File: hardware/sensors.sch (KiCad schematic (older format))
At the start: 19 parts, among them U1 LM358, U2 MCP6001, U3 LAH-100P, U4 LOC110, U5 MCP6001, U6 MCP6001

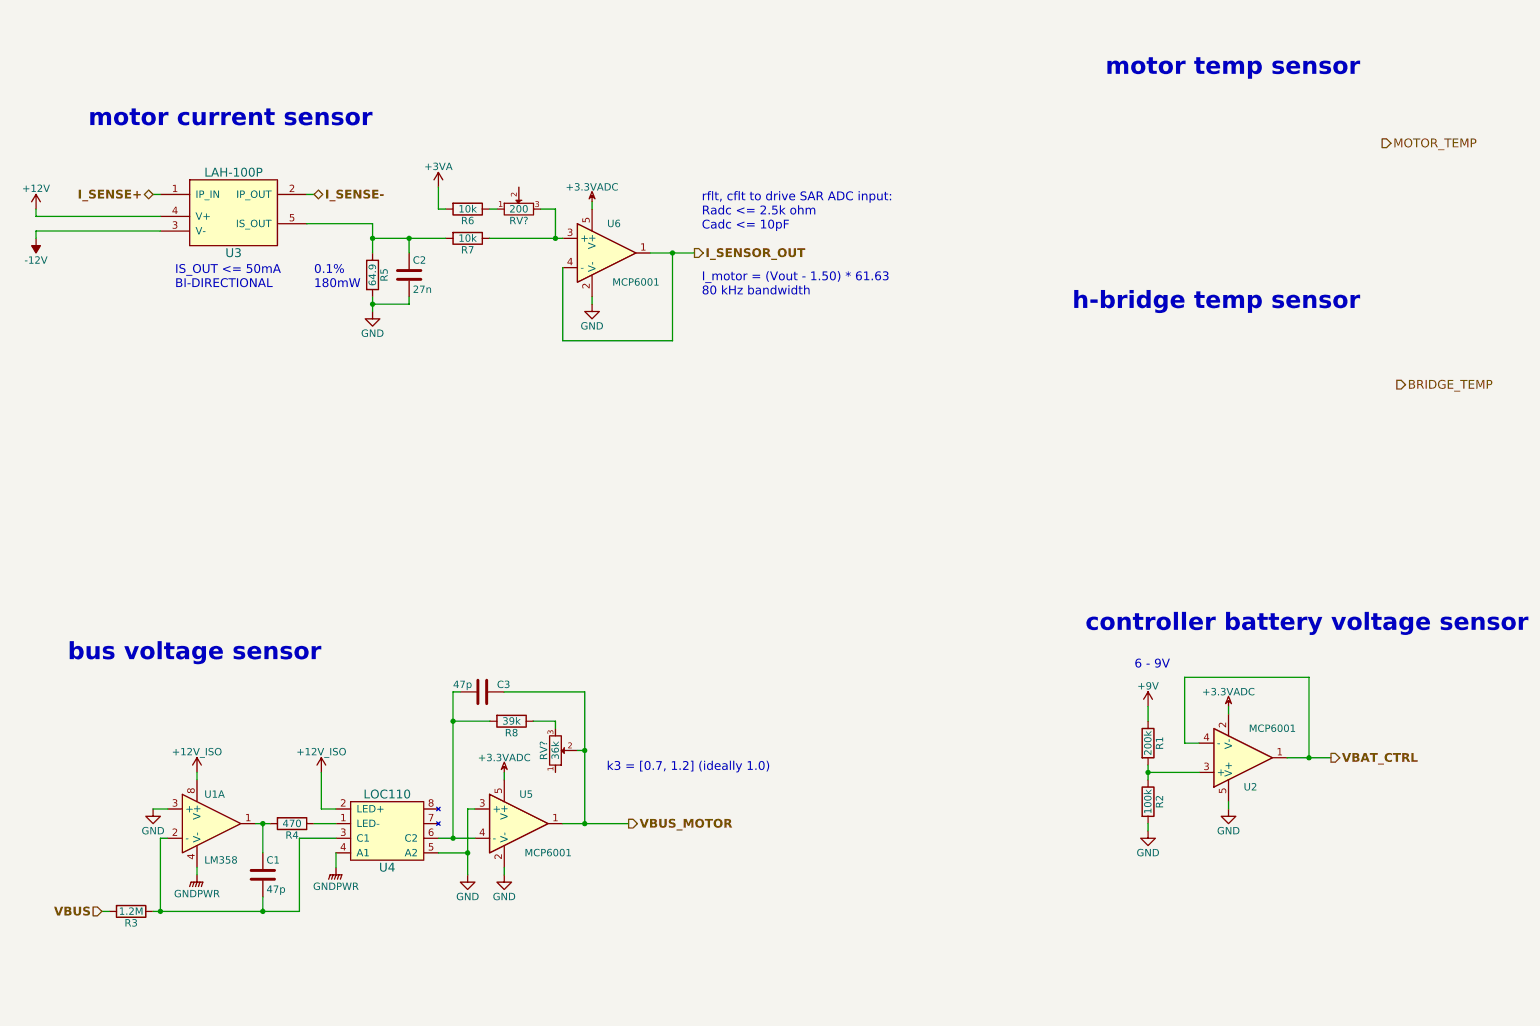
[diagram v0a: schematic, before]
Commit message: Update sensors, hbridge caps, add heatsink
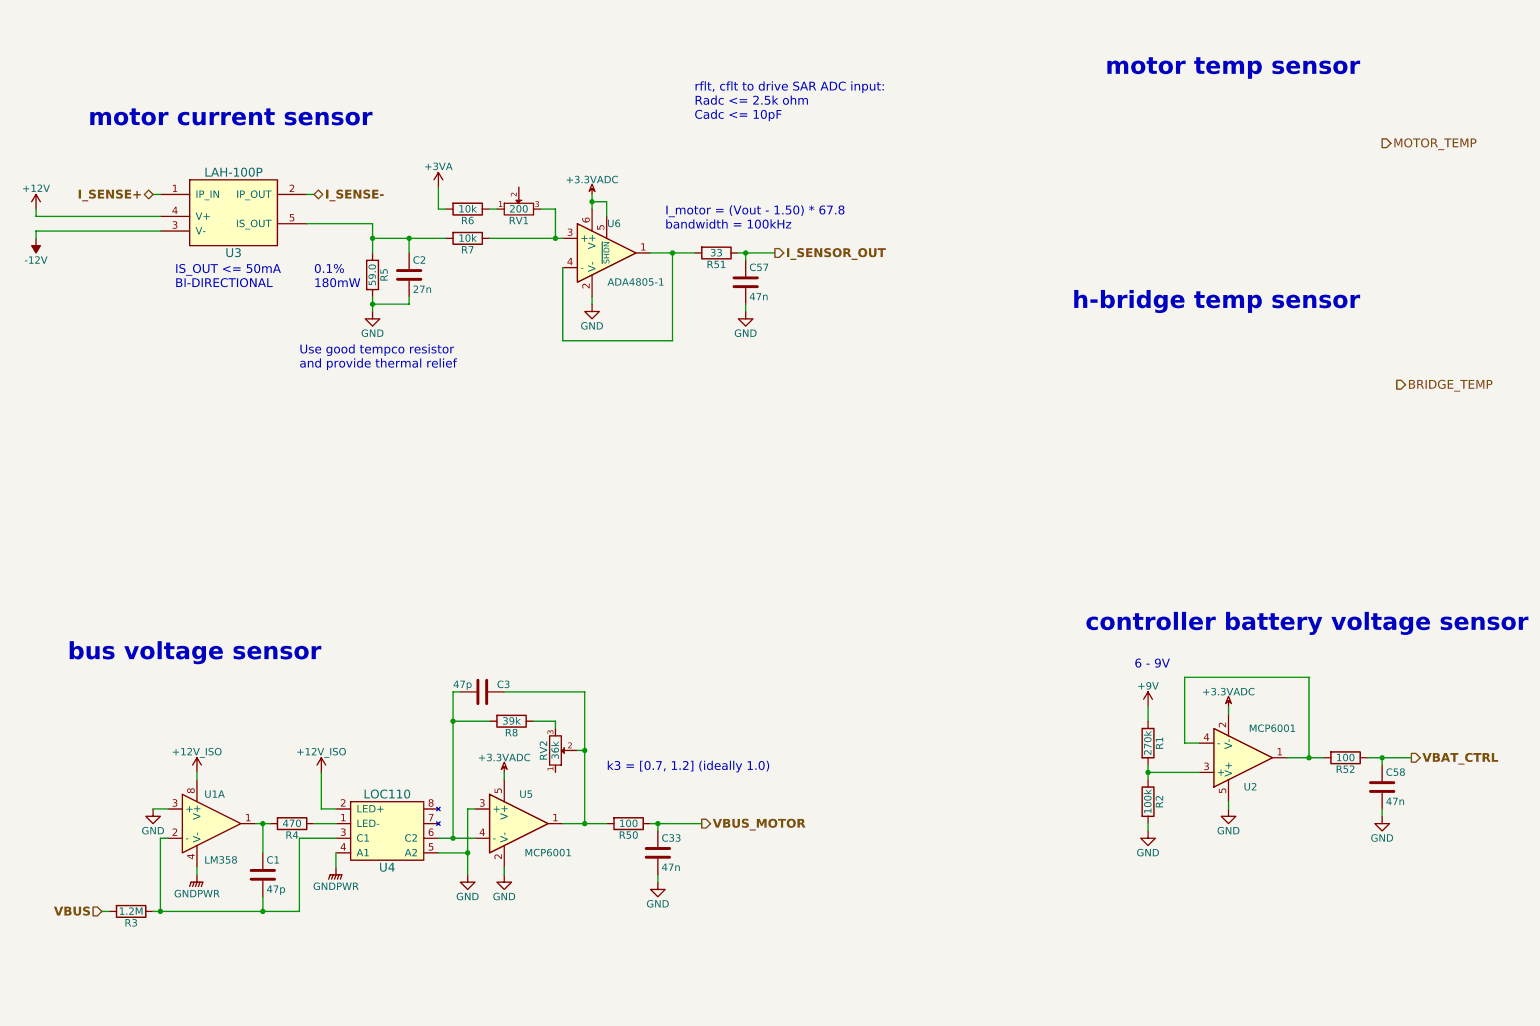
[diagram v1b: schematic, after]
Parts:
- removed U6: MCP6001, TO_SOT_Packages_SMD:SC-70-5, symbol MCP6001
- added C33, C57, C58: 47n, symbol C
- added R50, R52: 100, symbol R
- added R51: 33, symbol R
- added U6: ADA4805-1, symbol ADA4805-1
- R1: value 200k -> 270k
- R5: value 64.9 -> 59.0
- gave numbers to parts that had none: 2
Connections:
- net +3.3VADC: now also U6.5 (~SHDN), U6.6 (V+)
- net GND: now also C33.2, C57.2, C58.2, U6.2 (V-)
- net I_SENSOR_OUT: now also C57.1, R51.1
- net VBAT_CTRL: now also C58.1, R52.1; no longer U2.1, U2.4 (-)
- net VBUS_MOTOR: now also C33.1, R50.1; no longer C3.1, RV2.2, U5.1
- net at R7.1, RV1.3: now also U6.3 (+)
- new net: R52.2, U2.1, U2.4 (-)
- new net: C3.1, R50.2, RV2.2, U5.1
- new net: R51.2, U6.1, U6.4 (-)
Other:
- note added: "I_motor = (Vout - 1.50) * 67.8\nbandwidth = 100kHz"
- note added: "Use good tempco resistor\nand provide thermal relief"
- note removed: "I_motor = (Vout - 1.50) * 61.63\n80 kHz bandwidth"

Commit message: Layout first draft
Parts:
- C33, C57, C58: footprint (none) -> Capacitors_SMD:C_0603
- U6: footprint (none) -> TO_SOT_Packages_SMD:SOT-23-6
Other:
- note added: "0.05%\n180mW"
- note removed: "0.1%\n180mW"
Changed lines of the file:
@@
 I_motor = (Vout - 1.50) * 67.8\nbandwidth = 100kHz
 Text Notes 2750 2550 0    60   ~ 0
-0.1%\n180mW
+0.05%\n180mW
 $Comp
 L +3VA #PWR013
@@
 F 0 "C57" H 5725 2600 50  0000 L CNN
 F 1 "47n" H 5725 2400 50  0000 L CNN
-F 2 "" H 5738 2350 50  0001 C CNN
+F 2 "Capacitors_SMD:C_0603" H 5738 2350 50  0001 C CNN
 F 3 "" H 5700 2500 50  0000 C CNN
 	1    5700 2500
@@
 F 0 "U6" H 4800 2500 50  0000 C CNN
 F 1 "ADA4805-1" H 4950 2100 50  0000 C CNN
-F 2 "" H 4700 2400 50  0001 C CNN
+F 2 "TO_SOT_Packages_SMD:SOT-23-6" H 4700 2400 50  0001 C CNN
 F 3 "" H 4800 2500 50  0000 C CNN
 	1    4750 2300
@@
 F 0 "C33" H 5125 6500 50  0000 L CNN
 F 1 "47n" H 5125 6300 50  0000 L CNN
-F 2 "" H 5138 6250 50  0001 C CNN
+F 2 "Capacitors_SMD:C_0603" H 5138 6250 50  0001 C CNN
 F 3 "" H 5100 6400 50  0000 C CNN
 	1    5100 6400
@@
 F 0 "C58" H 10075 6050 50  0000 L CNN
 F 1 "47n" H 10075 5850 50  0000 L CNN
-F 2 "" H 10088 5800 50  0001 C CNN
+F 2 "Capacitors_SMD:C_0603" H 10088 5800 50  0001 C CNN
 F 3 "" H 10050 5950 50  0000 C CNN
 	1    10050 5950

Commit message: revised power layout
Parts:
- U3: footprint (none) -> 2kwMotorController:LAH_100-P
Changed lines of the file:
@@
 F 0 "U3" H 2200 1700 60  0000 C CNN
 F 1 "LAH-100P" H 2200 2250 60  0000 C CNN
-F 2 "" H 2200 2000 60  0001 C CNN
+F 2 "2kwMotorController:LAH_100-P" H 2200 2000 60  0001 C CNN
 F 3 "" H 2200 2000 60  0000 C CNN
 	1    2200 2000

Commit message: Added most footprints, did non-power layout
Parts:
- R50, R51, R52: footprint (none) -> Resistors_SMD:R_0603
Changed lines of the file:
@@
 F 0 "R51" V 5580 2300 50  0000 C CNN
 F 1 "33" V 5500 2300 50  0000 C CNN
-F 2 "" V 5430 2300 50  0001 C CNN
+F 2 "Resistors_SMD:R_0603" V 5430 2300 50  0001 C CNN
 F 3 "" H 5500 2300 50  0000 C CNN
 	1    5500 2300
@@
 F 0 "R50" V 4980 6200 50  0000 C CNN
 F 1 "100" V 4900 6200 50  0000 C CNN
-F 2 "" V 4830 6200 50  0001 C CNN
+F 2 "Resistors_SMD:R_0603" V 4830 6200 50  0001 C CNN
 F 3 "" H 4900 6200 50  0000 C CNN
 	1    4900 6200
@@
 F 0 "R52" V 9880 5750 50  0000 C CNN
 F 1 "100" V 9800 5750 50  0000 C CNN
-F 2 "" V 9730 5750 50  0001 C CNN
+F 2 "Resistors_SMD:R_0603" V 9730 5750 50  0001 C CNN
 F 3 "" H 9800 5750 50  0000 C CNN
 	1    9800 5750

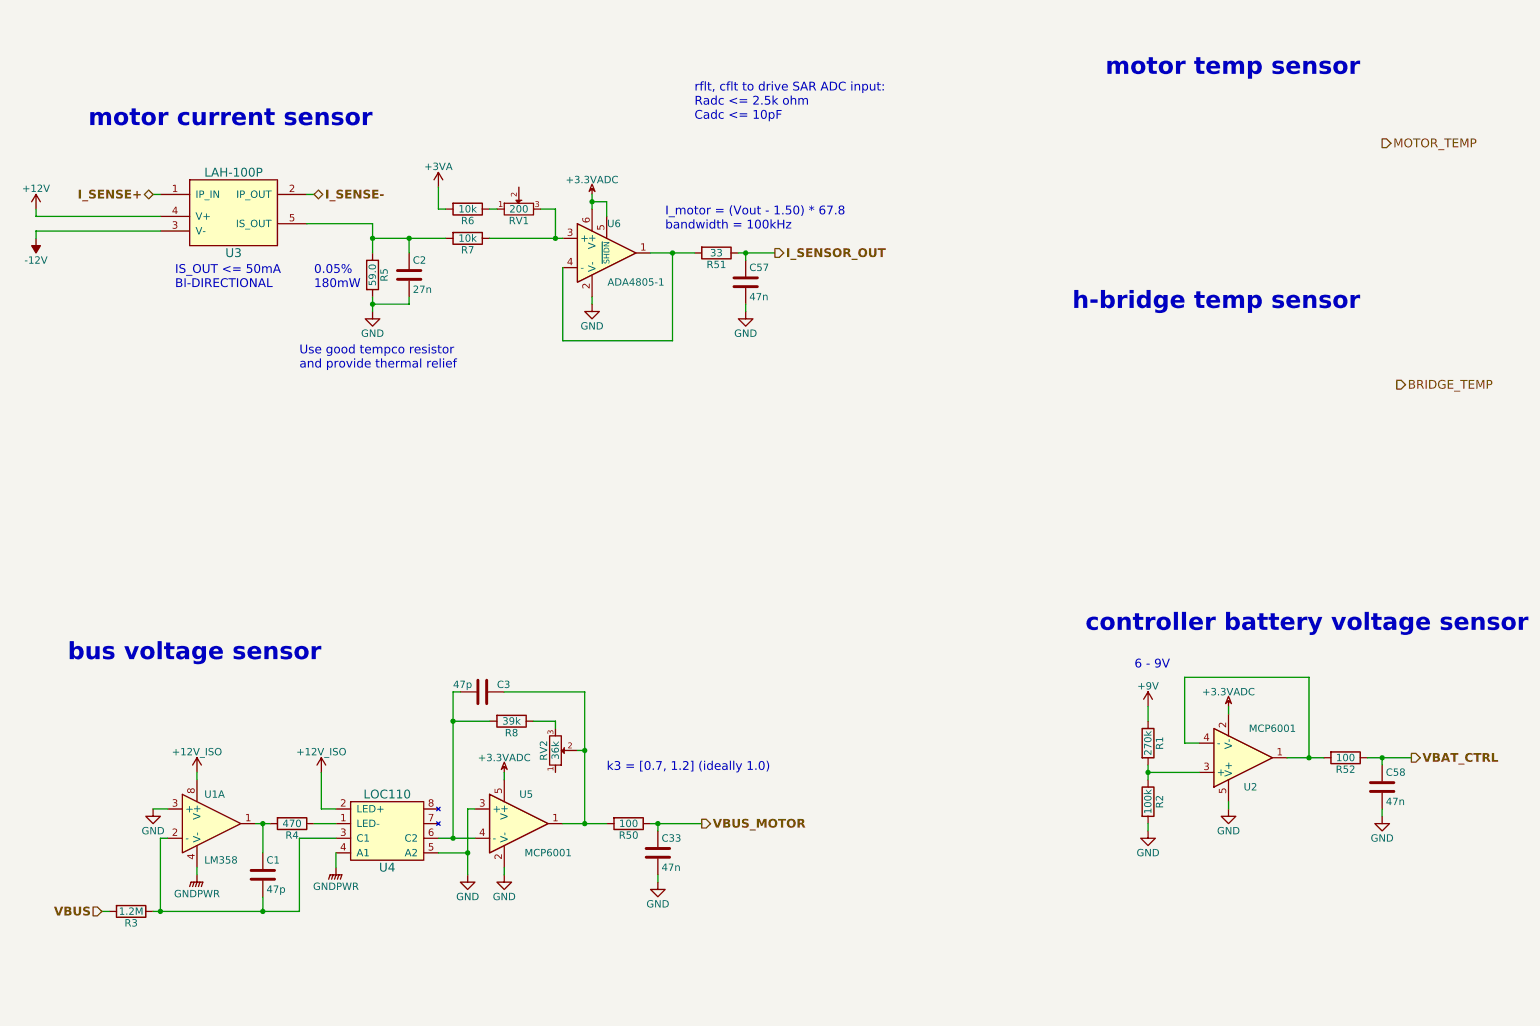
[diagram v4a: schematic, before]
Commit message: H-bridge decoupling, footprints, mechanical
- Finished H-bridge decoupling study and chose H-bridge caps
- Changed LT3471 inductors to those found in reference design,
  made footprints for them
- Swapped Si86xx isolator for Si80xx (smaller package)
- Updated heatsink footprint with correct screw sizes
- Created mechanical hole footprints (M3, M4 screws)
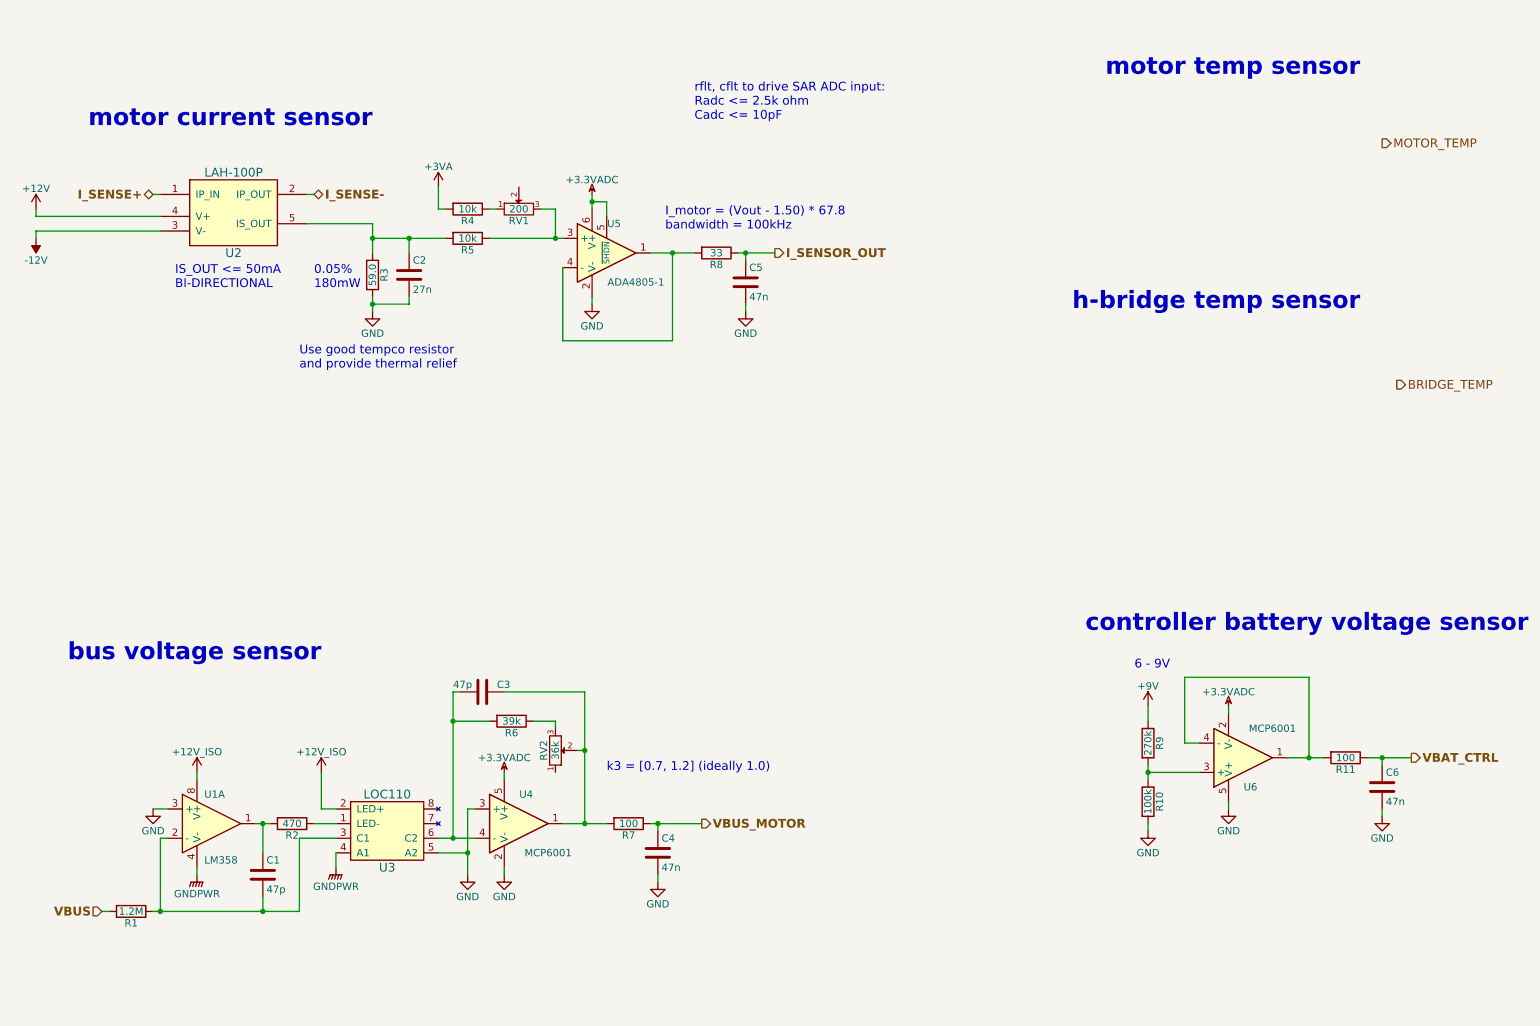
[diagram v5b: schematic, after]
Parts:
- renumbered C33 to C4, C57 to C5, C58 to C6, R3 to R1, R2 to R10, R52 to R11, R4 to R2, R5 to R3, R6 to R4, R7 to R5, R8 to R6, R50 to R7, R51 to R8, R1 to R9, U3 to U2, U4 to U3, U5 to U4, U6 to U5, U2 to U6
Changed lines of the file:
@@
 $EndDescr
 $Comp
-L LAH-100P U3
+L LAH-100P U2
 U 1 1 5975C20B
 P 2200 2000
-F 0 "U3" H 2200 1700 60  0000 C CNN
+F 0 "U2" H 2200 1700 60  0000 C CNN
 F 1 "LAH-100P" H 2200 2250 60  0000 C CNN
 F 2 "2kwMotorController:LAH_100-P" H 2200 2000 60  0001 C CNN
@@
 $EndComp
 $Comp
-L R R5
+L R R3
 U 1 1 5975C452
 P 3150 2450
-F 0 "R5" V 3230 2450 50  0000 C CNN
+F 0 "R3" V 3230 2450 50  0000 C CNN
 F 1 "59.0" V 3150 2450 50  0000 C CNN
 F 2 "Resistors_SMD:R_0603" V 3080 2450 50  0001 C CNN
@@
 $EndComp
 $Comp
-L R R7
+L R R5
 U 1 1 5975C99C
 P 3800 2200
-F 0 "R7" V 3880 2200 50  0000 C CNN
+F 0 "R5" V 3880 2200 50  0000 C CNN
 F 1 "10k" V 3800 2200 50  0000 C CNN
 F 2 "Resistors_SMD:R_0603" V 3730 2200 50  0001 C CNN
@@
 $EndComp
 $Comp
-L R R6
+L R R4
 U 1 1 5975CA28
 P 3800 2000
-F 0 "R6" V 3880 2000 50  0000 C CNN
+F 0 "R4" V 3880 2000 50  0000 C CNN
 F 1 "10k" V 3800 2000 50  0000 C CNN
 F 2 "Resistors_SMD:R_0603" V 3730 2000 50  0001 C CNN
@@
 6 - 9V
 $Comp
-L R R1
+L R R9
 U 1 1 597CFA75
 P 8450 5650
-F 0 "R1" V 8530 5650 50  0000 C CNN
+F 0 "R9" V 8530 5650 50  0000 C CNN
 F 1 "270k" V 8450 5650 50  0000 C CNN
 F 2 "Resistors_SMD:R_0603" V 8380 5650 50  0001 C CNN
@@
 $EndComp
 $Comp
-L R R2
+L R R10
 U 1 1 597CFAC7
 P 8450 6050
-F 0 "R2" V 8530 6050 50  0000 C CNN
+F 0 "R10" V 8530 6050 50  0000 C CNN
 F 1 "100k" V 8450 6050 50  0000 C CNN
 F 2 "Resistors_SMD:R_0603" V 8380 6050 50  0001 C CNN
@@
 $EndComp
 $Comp
-L MCP6001 U2
+L MCP6001 U6
 U 1 1 597CFF4C
 P 9100 5750
-F 0 "U2" H 9150 5950 50  0000 C CNN
+F 0 "U6" H 9150 5950 50  0000 C CNN
 F 1 "MCP6001" H 9300 5550 50  0000 C CNN
 F 2 "TO_SOT_Packages_SMD:SC-70-5" H 9050 5850 50  0001 C CNN
@@
 VBUS_MOTOR
 $Comp
-L R R4
+L R R2
 U 1 1 597E87B7
 P 2600 6200
-F 0 "R4" V 2680 6200 50  0000 C CNN
+F 0 "R2" V 2680 6200 50  0000 C CNN
 F 1 "470" V 2600 6200 50  0000 C CNN
 F 2 "Resistors_SMD:R_0603" V 2530 6200 50  0001 C CNN
@@
 $EndComp
 $Comp
-L LOC110 U4
+L LOC110 U3
 U 1 1 597E8D03
 P 3250 6250
-F 0 "U4" H 3250 6000 60  0000 C CNN
+F 0 "U3" H 3250 6000 60  0000 C CNN
 F 1 "LOC110" H 3250 6500 60  0000 C CNN
 F 2 "Housings_DIP:DIP-8_W7.62mm" H 3400 6050 60  0001 C CNN
@@
 $EndComp
 $Comp
-L R R3
+L R R1
 U 1 1 597E9880
 P 1500 6800
-F 0 "R3" V 1580 6800 50  0000 C CNN
+F 0 "R1" V 1580 6800 50  0000 C CNN
 F 1 "1.2M" V 1500 6800 50  0000 C CNN
 F 2 "Resistors_SMD:R_0603" V 1430 6800 50  0001 C CNN
@@
 $EndComp
 $Comp
-L MCP6001 U5
+L MCP6001 U4
 U 1 1 597EAA48
 P 4150 6200
-F 0 "U5" H 4200 6400 50  0000 C CNN
+F 0 "U4" H 4200 6400 50  0000 C CNN
 F 1 "MCP6001" H 4350 6000 50  0000 C CNN
 F 2 "TO_SOT_Packages_SMD:SC-70-5" H 4100 6300 50  0001 C CNN
@@
 $EndComp
 $Comp
-L R R8
+L R R6
 U 1 1 597EB265
 P 4100 5500
-F 0 "R8" V 4180 5500 50  0000 C CNN
+F 0 "R6" V 4180 5500 50  0000 C CNN
 F 1 "39k" V 4100 5500 50  0000 C CNN
 F 2 "Resistors_SMD:R_0603" V 4030 5500 50  0001 C CNN
@@
 Use good tempco resistor\nand provide thermal relief
 $Comp
-L R R51
+L R R8
 U 1 1 59B94C38
 P 5500 2300
-F 0 "R51" V 5580 2300 50  0000 C CNN
+F 0 "R8" V 5580 2300 50  0000 C CNN
 F 1 "33" V 5500 2300 50  0000 C CNN
 F 2 "Resistors_SMD:R_0603" V 5430 2300 50  0001 C CNN
@@
 $EndComp
 $Comp
-L C C57
+L C C5
 U 1 1 59B94C8F
 P 5700 2500
-F 0 "C57" H 5725 2600 50  0000 L CNN
+F 0 "C5" H 5725 2600 50  0000 L CNN
 F 1 "47n" H 5725 2400 50  0000 L CNN
 F 2 "Capacitors_SMD:C_0603" H 5738 2350 50  0001 C CNN
@@
 Connection ~ 5700 2300
 $Comp
-L ADA4805-1 U6
+L ADA4805-1 U5
 U 1 1 59B96B07
 P 4750 2300
-F 0 "U6" H 4800 2500 50  0000 C CNN
+F 0 "U5" H 4800 2500 50  0000 C CNN
 F 1 "ADA4805-1" H 4950 2100 50  0000 C CNN
 F 2 "TO_SOT_Packages_SMD:SOT-23-6" H 4700 2400 50  0001 C CNN
@@
 Connection ~ 4650 1950
 $Comp
-L R R50
+L R R7
 U 1 1 59B9903C
 P 4900 6200
-F 0 "R50" V 4980 6200 50  0000 C CNN
+F 0 "R7" V 4980 6200 50  0000 C CNN
 F 1 "100" V 4900 6200 50  0000 C CNN
 F 2 "Resistors_SMD:R_0603" V 4830 6200 50  0001 C CNN
@@
 $EndComp
 $Comp
-L C C33
+L C C4
 U 1 1 59B990C0
 P 5100 6400
-F 0 "C33" H 5125 6500 50  0000 L CNN
+F 0 "C4" H 5125 6500 50  0000 L CNN
 F 1 "47n" H 5125 6300 50  0000 L CNN
 F 2 "Capacitors_SMD:C_0603" H 5138 6250 50  0001 C CNN
@@
 Connection ~ 5100 6200
 $Comp
-L R R52
+L R R11
 U 1 1 59B9CA7D
 P 9800 5750
-F 0 "R52" V 9880 5750 50  0000 C CNN
+F 0 "R11" V 9880 5750 50  0000 C CNN
 F 1 "100" V 9800 5750 50  0000 C CNN
 F 2 "Resistors_SMD:R_0603" V 9730 5750 50  0001 C CNN
@@
 $EndComp
 $Comp
-L C C58
+L C C6
 U 1 1 59B9CA83
 P 10050 5950
-F 0 "C58" H 10075 6050 50  0000 L CNN
+F 0 "C6" H 10075 6050 50  0000 L CNN
 F 1 "47n" H 10075 5850 50  0000 L CNN
 F 2 "Capacitors_SMD:C_0603" H 10088 5800 50  0001 C CNN
